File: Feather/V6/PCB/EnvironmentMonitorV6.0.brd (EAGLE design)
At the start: 73 x 73 mm, 64 parts, among them IC1 BME680, IC2 TCS3472, IC3 CCS811, IC5 FEATHERWING_NODIM, Q1 IRFML8244TRPBF, U1 GRIDEYE, U2 LMV358, U3 LIS3DH

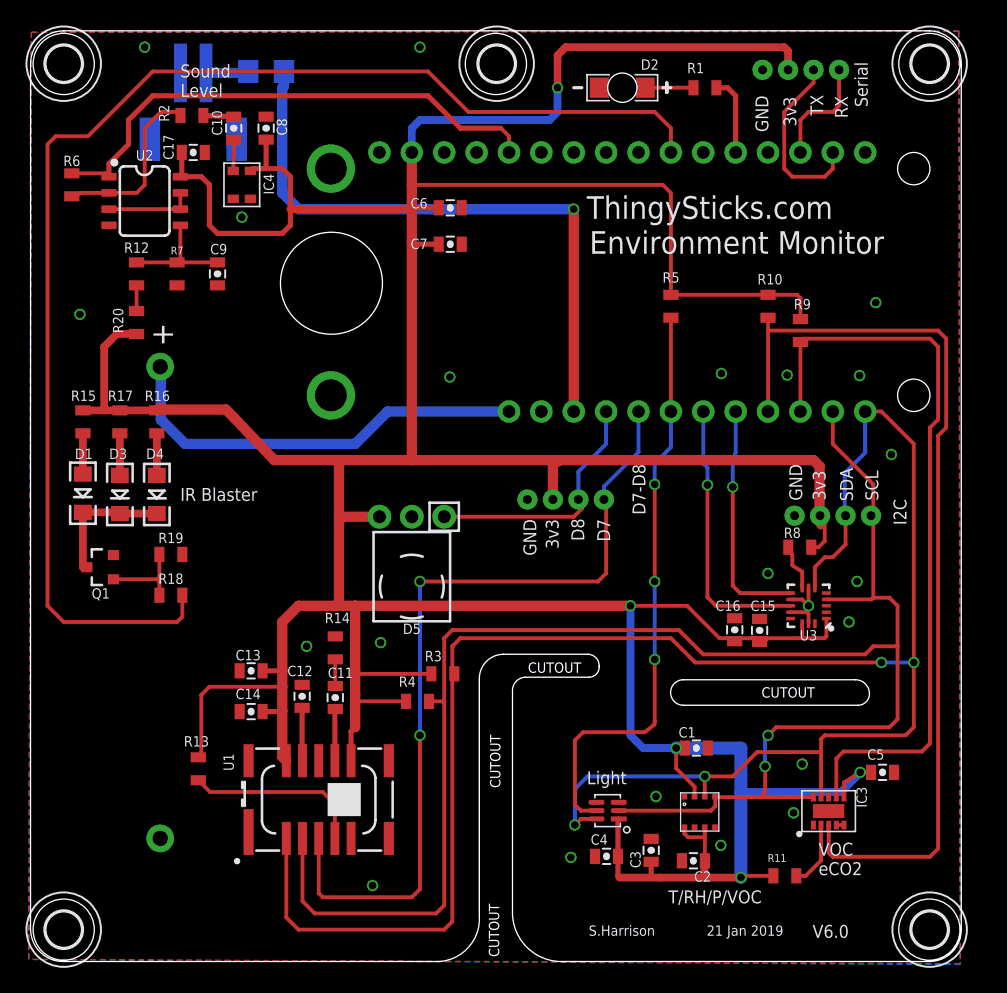
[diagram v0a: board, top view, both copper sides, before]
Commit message: Modified mounting holes to smaller size to match enclosure.
Modified cutout so it's a larger continious section.

Updated images from DirtyPCBs

Added image exports from Eagle.

Boards updated at DirtyPCBs.
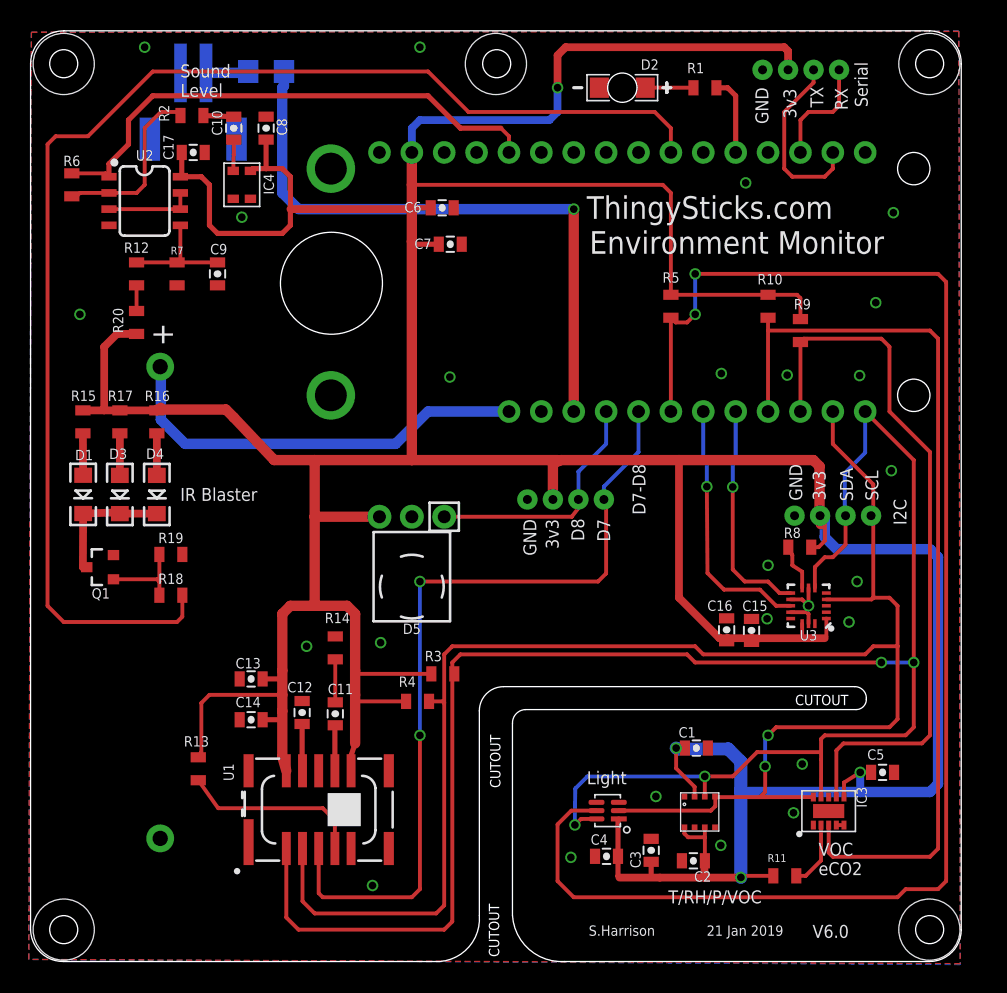
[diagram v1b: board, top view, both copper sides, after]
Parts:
- removed H1, H2, H3, H4, H5: MOUNT-HOLE2.8, holes:2,8
- moved C11 1.27 mm to (21.3, 16.9)
- moved C12 1.27 mm to (18.7, 17.0)
- moved U1 0.79 mm to (20.0, 9.41)
- moved C15 0.64 mm to (53.9, 23.5)
- moved C13 0.64 mm to (14.7, 19.7)
- moved C14 0.64 mm to (14.7, 16.5)
- moved C6 0.64 mm to (29.7, 56.6)
- moved C16 0.63 mm to (52.0, 23.5)
- moved D1 0.09 mm to (1.52, 34.1)
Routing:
- net LIGHT_INT: track 46.1 -> 119.3 mm, vias 3 -> 2
- net 3.3V: track 412.3 -> 418.4 mm, vias 5 -> 4
- net SDA: track 161.2 -> 157.8 mm
- net CCS_WAKE: track 58.8 -> 56.1 mm
- net SCL: track 138.7 -> 136.2 mm
- net N$16: track 2.10 -> 3.37 mm
- net ACCEL_INT1: track 21.5 -> 20.4 mm
- net CCS_INT: track 73.0 -> 72.1 mm
- net GRIDEYE_INT: track 65.5 -> 64.7 mm
- net ACCEL_INT2: track 18.5 -> 17.8 mm
- net GND: vias 22 -> 25
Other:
- outline, holes or cut-outs redrawn

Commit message: Added values and corrected filename for export script
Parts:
- R5: value (none) -> 10k
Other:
- board text added: ". mark on Anode"
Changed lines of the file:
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@@
 <hole x="0" y="67.92" drill="2.2"/>
 <text x="58.41" y="0.37" size="1.016" layer="26" font="vector" ratio="15" rot="MR180">V6.0</text>
+<text x="8.89" y="36.195" size="1.016" layer="51">. mark on Anode</text>
 </plain>
 <attributes>
@@
 <attribute name="VALUE" x="41.559" y="4.353" size="0.4064" layer="27"/>
 </element>
-<element name="R5" library="SparkFun-Resistors" package="0805" value=" " x="47.625" y="48.895" smashed="yes" rot="R90">
+<element name="R5" library="SparkFun-Resistors" package="0805" value="10k" x="47.625" y="48.895" smashed="yes" rot="R90">
 <attribute name="NAME" x="46.9646" y="50.7492" size="0.8128" layer="25" ratio="15"/>
 <attribute name="VALUE" value=" " x="46.482" y="47.879" size="0.4064" layer="27" rot="R90"/>
